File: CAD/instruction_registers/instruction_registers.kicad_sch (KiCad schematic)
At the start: 57 parts, among them J1 Conn_01x32_Pin, J2 Conn_01x06_Pin, SW1 SW_Push, SW2 SW_Push, SW3 SW_SPDT, U1 74HC377, U2 74HC377, U3 74HC377, U4 74HC245, U5 74HC245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

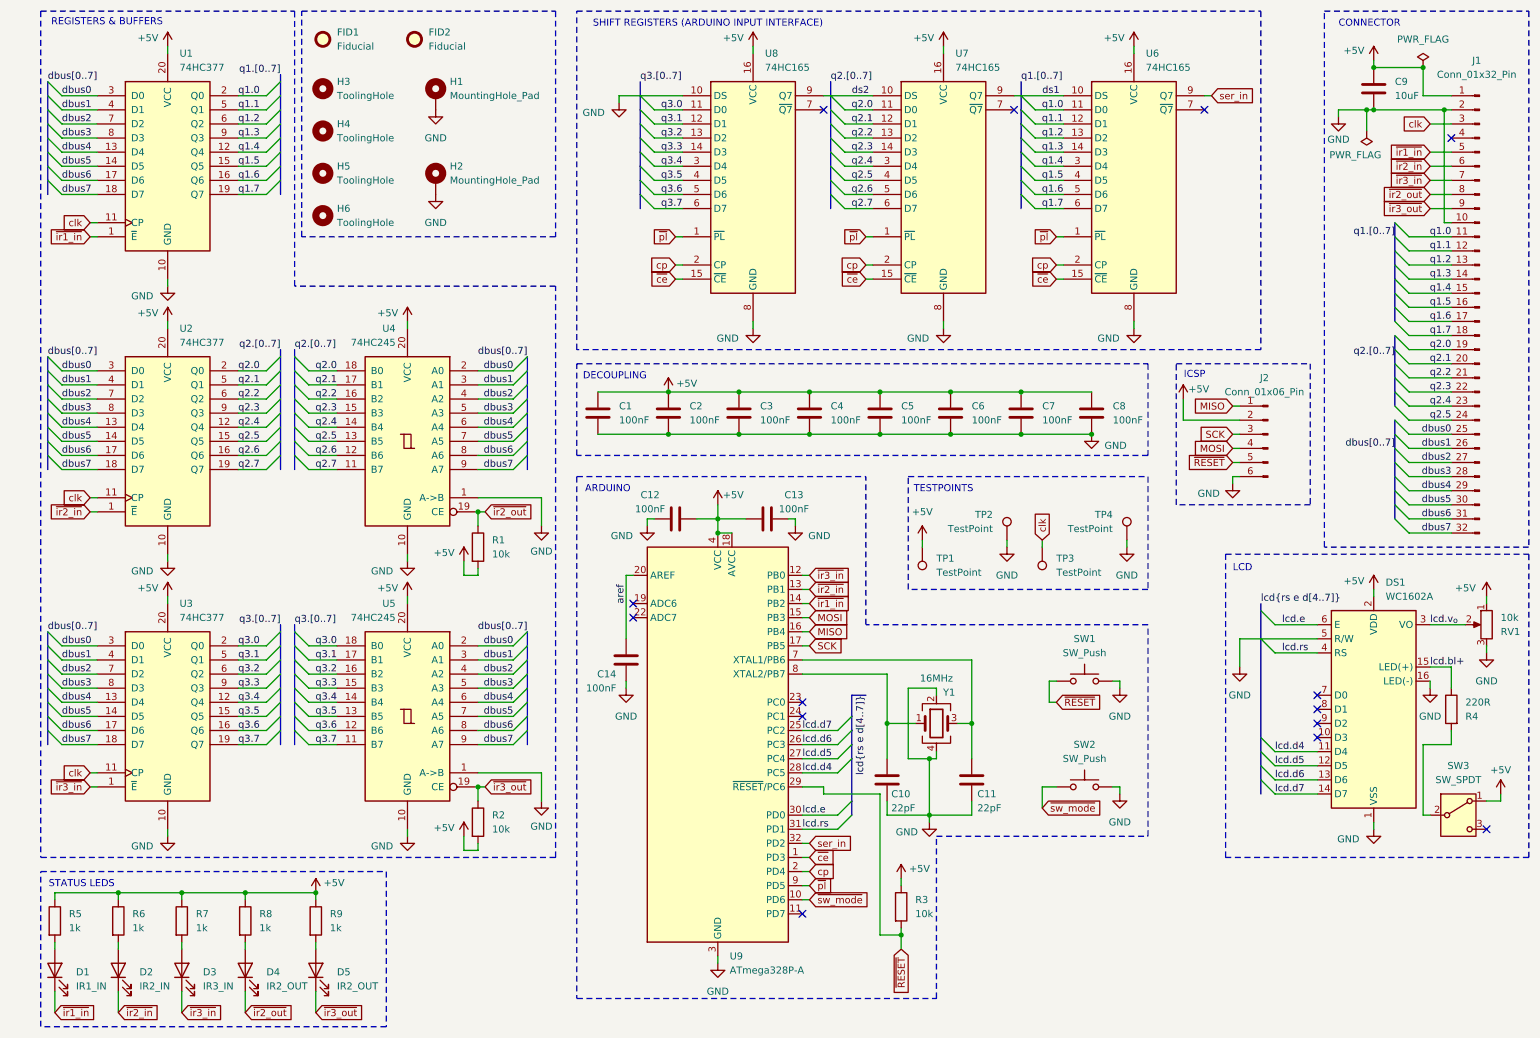
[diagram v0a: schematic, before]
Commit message: update IR, move crystal, change capacitors, add testpoints, ground planes
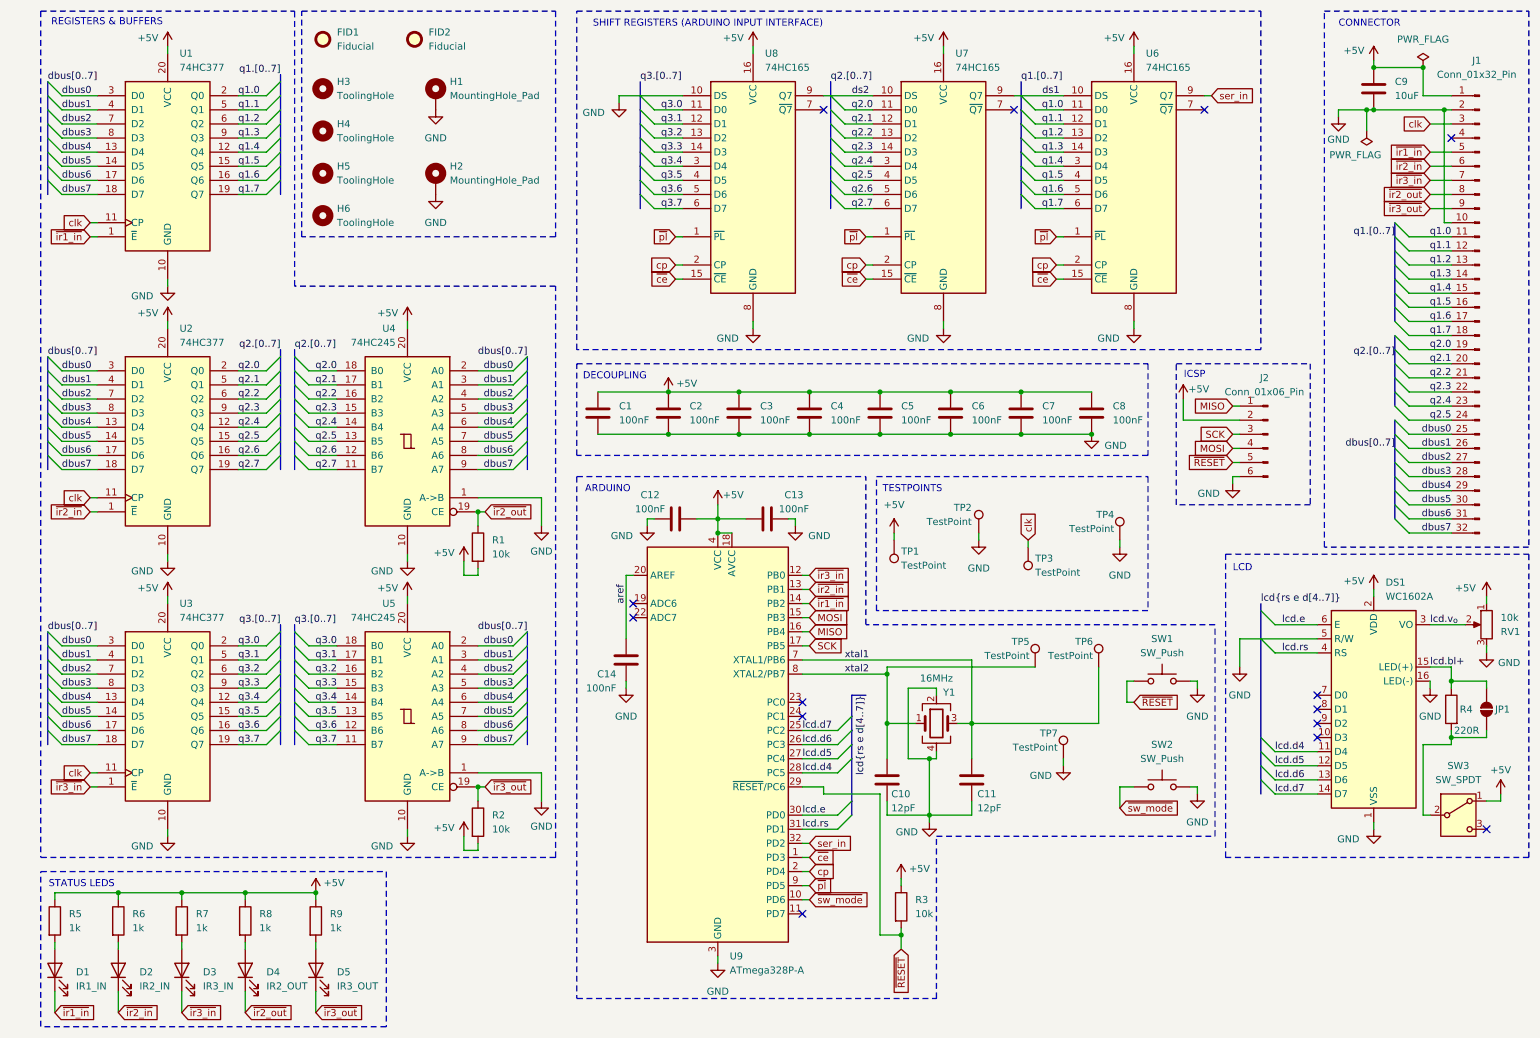
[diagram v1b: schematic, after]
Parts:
- added JP1: SolderJumper_2_Open, Jumper:SolderJumper-2_P1.3mm_Open_RoundedPad1.0x1.5mm, symbol Jumper:SolderJumper_2_Open
- added TP5, TP6, TP7: TestPoint, TestPoint:TestPoint_THTPad_D1.0mm_Drill0.5mm, symbol Connector:TestPoint
- C1, C12, C13, C14, C2, C3, C4, C5, C6, C7, C8: LCSC (none) -> C28233
- C10, C11: value 22pF -> 12pF; LCSC (none) -> C1792
- C9: LCSC (none) -> C15850
- D1, D2, D3: LCSC (none) -> C2297
- D4: LCSC (none) -> C2296
- D5: value IR2_OUT -> IR3_OUT; LCSC (none) -> C2296
- DS1, J2, TP1, TP2, TP3, TP4: now left out of the parts list
- J1: LCSC (none) -> C18905914
- R1, R2, R3: LCSC (none) -> C17414
- R4: LCSC (none) -> C17557
- R5, R6, R7, R8, R9: LCSC (none) -> C17513
- RV1: Details (none) -> https://www.lcsc.com/product-detail/C36376.html; LCSC (none) -> C36376
- SW1, SW2: Details (none) -> https://jlcpcb.com/partdetail/XKBConnection-TS_1187A_B_AB/C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; LCSC (none) -> C318884
- SW3: Details (none) -> https://www.lcsc.com/product-detail/C221841.html; LCSC (none) -> C221841
- U9: Details (none) -> https://jlcpcb.com/partdetail/MicrochipTech-ATMEGA328PAU/C1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; LCSC (none) -> C14877
- Y1: Details (none) -> https://jlcpcb.com/partdetail/YXC_CrystalOscillators-X32251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; LCSC (none) -> C13738
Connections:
- net GND: now also TP7.1
- net lcd.bl+: now also JP1.2 (B)
- net at R4.2, SW3.2 (B): now also JP1.1 (A)
- net xtal1: now reaches C11.1, U9.7 (XTAL1/PB6), Y1.3
- net xtal1: now also TP6.1
- net xtal2: now reaches C10.1, U9.8 (XTAL2/PB7), Y1.1
- net xtal2: now also TP5.1
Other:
- moved on the sheet: SW1, SW2, TP1, TP2, TP3, TP4

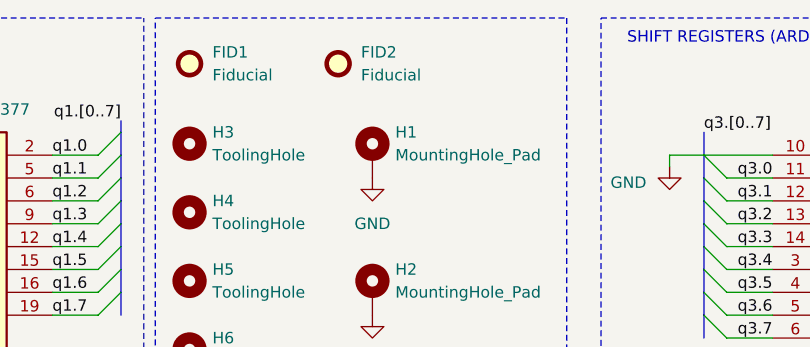
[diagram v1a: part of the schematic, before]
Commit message: IR layout changes
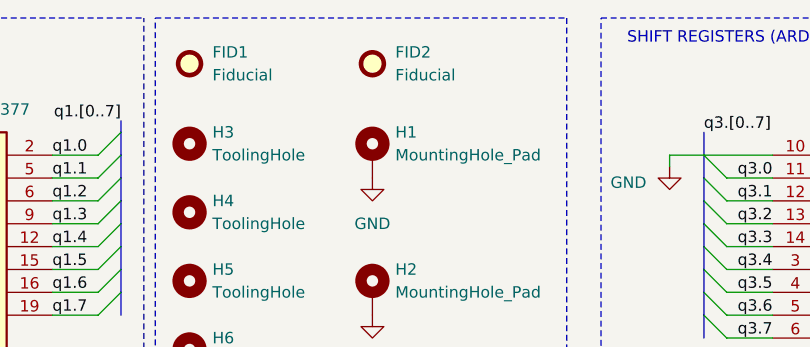
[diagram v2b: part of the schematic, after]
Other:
- moved on the sheet: FID2
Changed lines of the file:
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@@
 		)
 		(instances
-			(project ""
+			(project "instruction_registers"
 				(path "/4251315d-5042-4624-83d8-1c3574ca551e"
 					(reference "#PWR033")
@@
 		)
 		(instances
-			(project ""
+			(project "instruction_registers"
 				(path "/4251315d-5042-4624-83d8-1c3574ca551e"
 					(reference "D1")
@@
 		)
 		(instances
-			(project ""
+			(project "instruction_registers"
 				(path "/4251315d-5042-4624-83d8-1c3574ca551e"
 					(reference "U1")
@@
 		)
 		(instances
-			(project ""
+			(project "instruction_registers"
 				(path "/4251315d-5042-4624-83d8-1c3574ca551e"
 					(reference "#PWR024")
@@
 		)
 		(instances
-			(project ""
+			(project "instruction_registers"
 				(path "/4251315d-5042-4624-83d8-1c3574ca551e"
 					(reference "SW3")
@@
 		)
 		(instances
-			(project ""
+			(project "instruction_registers"
 				(path "/4251315d-5042-4624-83d8-1c3574ca551e"
 					(reference "U6")
@@
 		)
 		(instances
-			(project ""
+			(project "instruction_registers"
 				(path "/4251315d-5042-4624-83d8-1c3574ca551e"
 					(reference "JP1")
@@
 		)
 		(instances
-			(project ""
+			(project "instruction_registers"
 				(path "/4251315d-5042-4624-83d8-1c3574ca551e"
 					(reference "U9")
@@
 		)
 		(instances
-			(project ""
+			(project "instruction_registers"
 				(path "/4251315d-5042-4624-83d8-1c3574ca551e"
 					(reference "DS1")
@@
 	(symbol
 		(lib_id "Mechanical:Fiducial")
-		(at 81.28 17.78 0)
+		(at 85.09 17.78 0)
 		(unit 1)
 		(exclude_from_sim no)
@@
 		(fields_autoplaced yes)
 		(property "Reference" "FID2"
-			(at 83.82 16.5099 0)
+			(at 87.63 16.5099 0)
 			(effects
 				(font
@@
 		)
 		(property "Value" "Fiducial"
-			(at 83.82 19.0499 0)
+			(at 87.63 19.0499 0)
 			(effects
 				(font
@@
 		)
 		(property "Footprint" "Fiducial:Fiducial_0.5mm_Mask1mm"
-			(at 81.28 17.78 0)
+			(at 85.09 17.78 0)
 			(effects
 				(font
@@
 		)
 		(property "Datasheet" "~"
-			(at 81.28 17.78 0)
+			(at 85.09 17.78 0)
 			(effects
 				(font
@@
 		)
 		(property "Description" "Fiducial Marker"
-			(at 81.28 17.78 0)
+			(at 85.09 17.78 0)
 			(effects
 				(font
@@
 		)
 		(instances
-			(project ""
+			(project "instruction_registers"
 				(path "/4251315d-5042-4624-83d8-1c3574ca551e"
 					(reference "#PWR039")
@@
 		)
 		(instances
-			(project ""
+			(project "instruction_registers"
 				(path "/4251315d-5042-4624-83d8-1c3574ca551e"
 					(reference "#PWR01")
@@
 		)
 		(instances
-			(project ""
+			(project "instruction_registers"
 				(path "/4251315d-5042-4624-83d8-1c3574ca551e"
 					(reference "R1")
@@
 		)
 		(instances
-			(project ""
+			(project "instruction_registers"
 				(path "/4251315d-5042-4624-83d8-1c3574ca551e"
 					(reference "J2")
@@
 		)
 		(instances
-			(project ""
+			(project "instruction_registers"
 				(path "/4251315d-5042-4624-83d8-1c3574ca551e"
 					(reference "RV1")
@@
 		)
 		(instances
-			(project ""
+			(project "instruction_registers"
 				(path "/4251315d-5042-4624-83d8-1c3574ca551e"
 					(reference "#PWR016")
@@
 		)
 		(instances
-			(project ""
+			(project "instruction_registers"
 				(path "/4251315d-5042-4624-83d8-1c3574ca551e"
 					(reference "C10")
@@
 		)
 		(instances
-			(project ""
+			(project "instruction_registers"
 				(path "/4251315d-5042-4624-83d8-1c3574ca551e"
 					(reference "Y1")
@@
 		)
 		(instances
-			(project ""
+			(project "instruction_registers"
 				(path "/4251315d-5042-4624-83d8-1c3574ca551e"
 					(reference "SW1")
@@
 		)
 		(instances
-			(project ""
+			(project "instruction_registers"
 				(path "/4251315d-5042-4624-83d8-1c3574ca551e"
 					(reference "C1")
@@
 		)
 		(instances
-			(project ""
+			(project "instruction_registers"
 				(path "/4251315d-5042-4624-83d8-1c3574ca551e"
 					(reference "R5")
@@
 		)
 		(instances
-			(project ""
+			(project "instruction_registers"
 				(path "/4251315d-5042-4624-83d8-1c3574ca551e"
 					(reference "#PWR017")
@@
 		)
 		(instances
-			(project ""
+			(project "instruction_registers"
 				(path "/4251315d-5042-4624-83d8-1c3574ca551e"
 					(reference "#PWR043")
@@
 		)
 		(instances
-			(project ""
+			(project "instruction_registers"
 				(path "/4251315d-5042-4624-83d8-1c3574ca551e"
 					(reference "#PWR02")
@@
 		)
 		(instances
-			(project ""
+			(project "instruction_registers"
 				(path "/4251315d-5042-4624-83d8-1c3574ca551e"
 					(reference "#PWR038")
@@
 		)
 		(instances
-			(project ""
+			(project "instruction_registers"
 				(path "/4251315d-5042-4624-83d8-1c3574ca551e"
 					(reference "#FLG01")
@@
 		)
 		(instances
-			(project ""
+			(project "instruction_registers"
 				(path "/4251315d-5042-4624-83d8-1c3574ca551e"
 					(reference "U4")

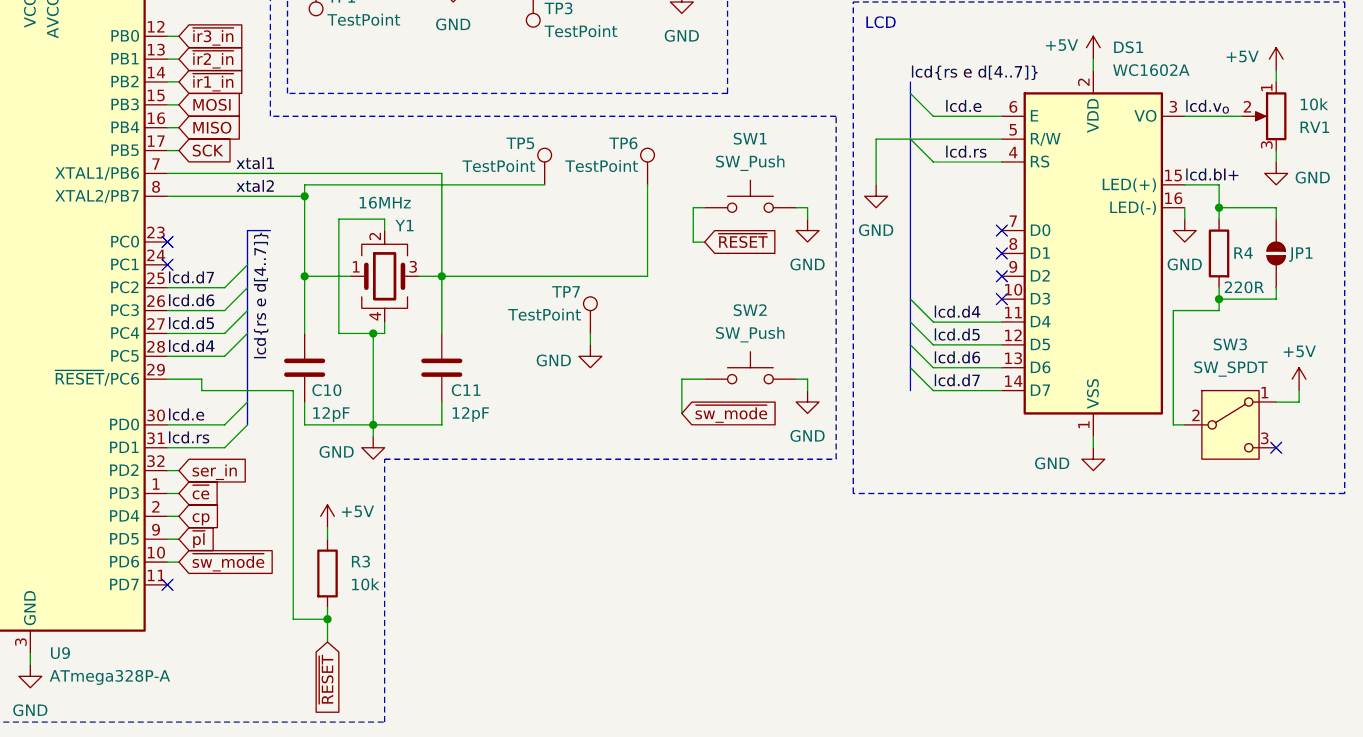
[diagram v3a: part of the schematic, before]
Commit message: exclude known warnings in ERC and DRC
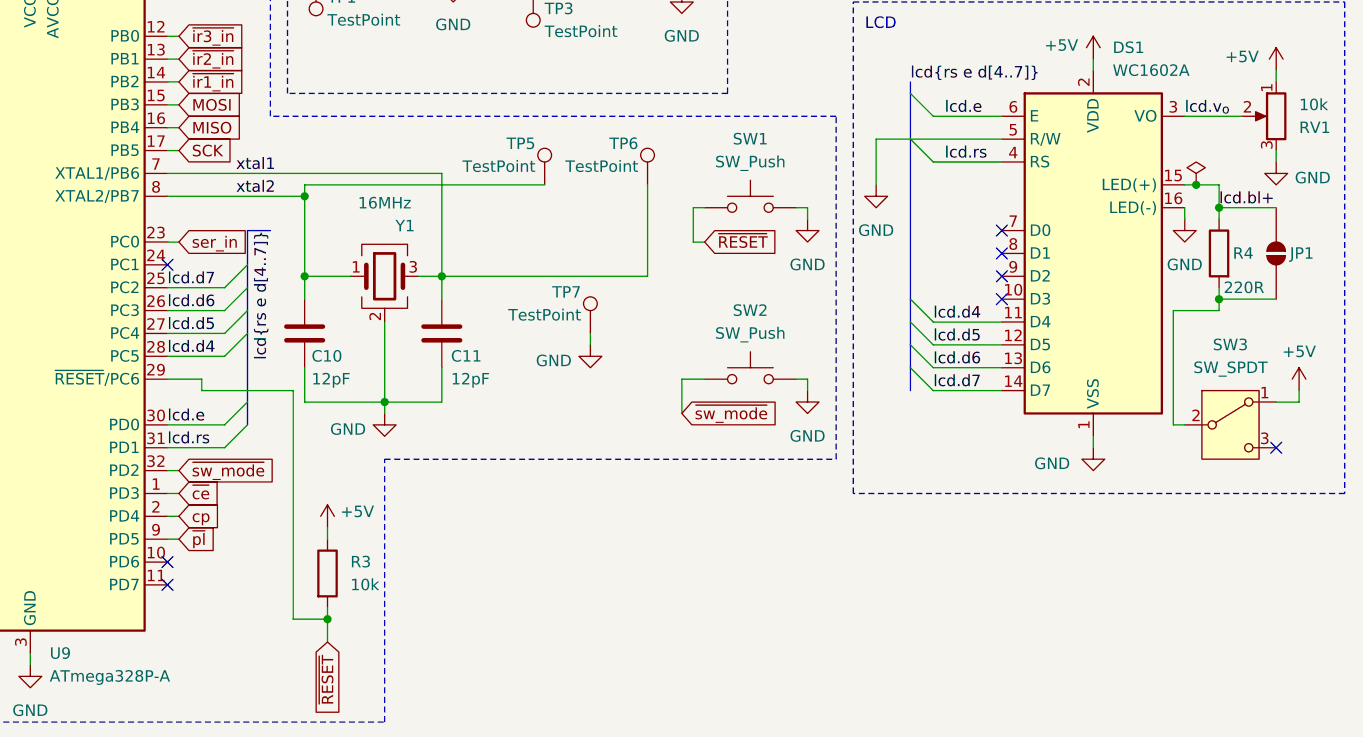
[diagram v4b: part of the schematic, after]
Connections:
- net ser_in: now also U9.23 (PC0); no longer U9.32 (PD2)
- net ~{sw_mode}: now also U9.32 (PD2); no longer U9.10 (PD6)
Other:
- moved on the sheet: C10, C11
